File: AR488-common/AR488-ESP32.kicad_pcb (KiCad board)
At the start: 2 copper layers, 63.5 x 40.6 mm, 9 parts, among them J1 Conn_02x12_Top_Bottom, J2 Conn_02x12_Odd_Even, J3 Barrel_Jack, J4 Screw_Terminal_01x02, U2 SN75162, U3 SN75160BDW

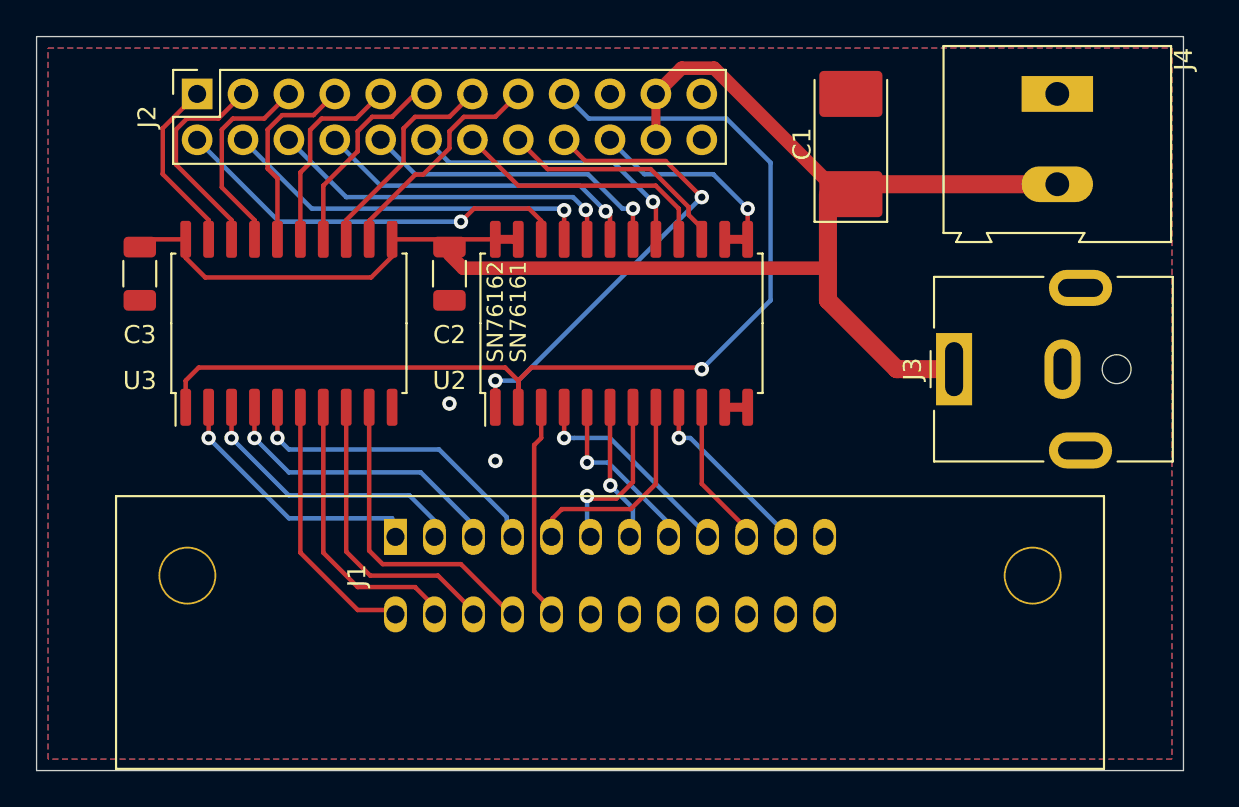
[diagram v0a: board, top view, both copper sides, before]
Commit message: Better pin assignment for the inter-PCB connector
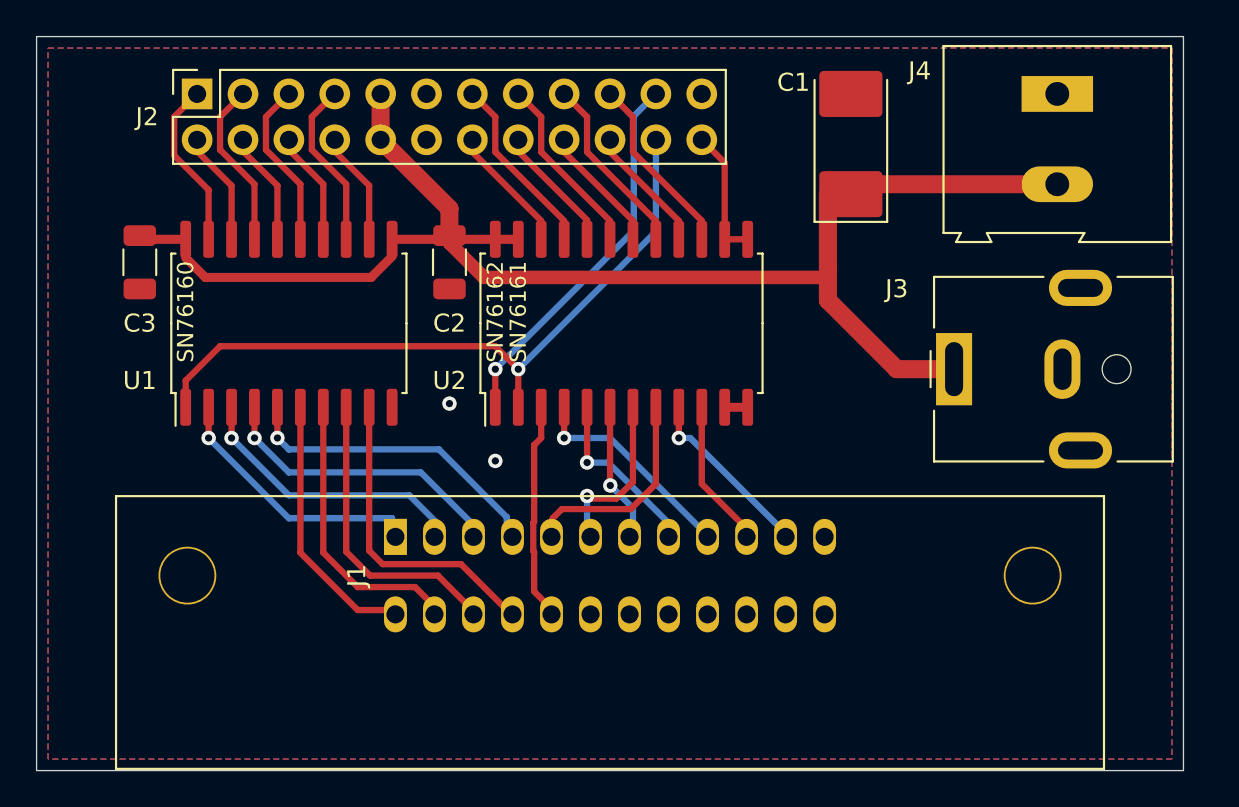
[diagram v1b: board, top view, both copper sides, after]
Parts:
- J1: value Conn_02x12_Top_Bottom -> GPIB-24
- U2: value SN75162 -> SN75162BDW
- moved C2 0.64 mm to (175.3, 82.3)
- moved C3 0.64 mm to (158.1, 82.3)
- renumbered U3 to U1
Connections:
- J2 pad 10: DAV_a -> +5V
- J2 pad 11: D6 -> GND
- J2 pad 12: EOI_a -> GND
- J2 pad 13: D7 -> IFC_a
- J2 pad 14: ATN_a -> REN_a
- J2 pad 15: D8 -> NRFD_a
- J2 pad 16: SRQ_a -> NDAC_a
- J2 pad 17: TE -> EOI_a
- J2 pad 18: SC -> DAV_a
- J2 pad 19: GND -> SRQ_a
- J2 pad 2: REN_a -> D2
- J2 pad 20: DC -> ATN_a
- J2 pad 21: +5V -> SC
- J2 pad 22: +5V -> TE
- J2 pad 24: GND -> DC
- J2 pad 3: D2 -> D3
- J2 pad 4: IFC_a -> D4
- J2 pad 5: D3 -> D5
- J2 pad 6: NDAC_a -> D6
- J2 pad 7: D4 -> D7
- J2 pad 8: NRFD_a -> D8
- J2 pad 9: D5 -> +5V
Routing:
- net TE: track 60.0 -> 39.0 mm
- net REN_a: track 22.5 -> 7.09 mm, vias 1 -> 0
- net NDAC_a: track 19.7 -> 6.45 mm, vias 1 -> 0
- net IFC_a: track 21.0 -> 10.2 mm, vias 1 -> 0
- net DAV_a: track 17.2 -> 7.09 mm, vias 1 -> 0
- net NRFD_a: track 18.3 -> 10.2 mm, vias 2 -> 0
- net ATN_a: track 14.7 -> 7.09 mm
- net D8: track 12.7 -> 6.30 mm
- net EOI_a: track 16.1 -> 10.2 mm, vias 1 -> 0
- net DC: track 12.5 -> 7.10 mm, vias 1 -> 0
- net D2: track 11.5 -> 6.30 mm
- net D6: track 11.4 -> 6.30 mm
- net SC: track 25.8 -> 20.8 mm, vias 2 -> 1
- net +5V: track 88.7 -> 83.7 mm
- net D4: track 10.8 -> 6.30 mm
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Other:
- board text added: "SN76160"
